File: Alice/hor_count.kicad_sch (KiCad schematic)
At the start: 267 parts, among them Q1 PASS, Q159 NOT_OC, Q160 NOT_OC, Q161 NOT_OC, Q162 NOT_OC, Q163 NOT_OC, Q164 NOT_OC, Q165 NOT_OC, Q166 NOT_OC, Q167 NOT_OC, Q168 NOT_OC, Q169 NOT_OC, Q170 NOT_OC, Q171 NOT_OC, Q172 NOT_OC, Q173 NOT_OC, Q174 NOT_OC, Q175 NOT_OC, Q176 NOT_OC, Q177 NOT_OC, Q178 NOT_OC, Q179 NOT_OC, Q180 NOT_OC, Q181 NOT_OC, Q182 NOT_OC, Q183 NOT_OC, Q184 NOT_OC, Q185 NOT_OC, Q186 NOT_OC, Q187 NOT_OC, Q188 NOT_OC, Q189 NOT_OC, Q190 NOT_OC, Q191 NOT_OC, Q192 NOT_OC, Q193 NOT_OC, Q194 NOT_OC, Q195 NOT_OC, Q196 NOT_OC, Q197 NOT_OC, Q198 NOT_OC, Q199 NOT_OC, Q2 PASS, Q200 NOT_OC, Q201 NOT_OC, Q202 NOT_OC, Q203 NOT_OC, Q204 NOT_OC, Q205 NOT_OC, Q206 NOT_OC, Q207 NOT_OC, Q208 NOT_OC, Q209 NOT_OC, Q210 NOT_OC, Q211 NOT_OC, Q212 NOT_OC, Q213 NOT_OC, Q214 NOT_OC, Q215 NOT_OC, Q216 NOT_OC, Q217 NOT_OC, Q218 NOT_OC, Q219 NOT_OC, Q220 NOT_OC, Q221 NOT_OC, Q222 NOT_OC, Q223 NOT_OC, Q224 NOT_OC, Q225 NOT_OC, Q226 NOT_OC, Q227 NOT_OC, Q228 NOT_OC, Q229 NOT_OC, Q230 NOT_OC, Q231 NOT_OC, Q232 NOT_OC, Q233 NOT_OC, Q234 NOT_OC, Q235 NOT_OC, Q236 NOT_OC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

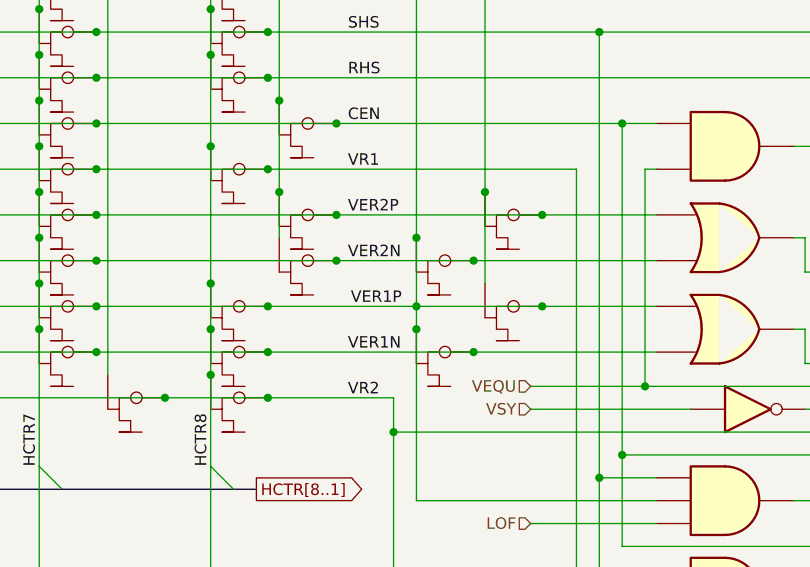
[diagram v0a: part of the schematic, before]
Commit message: Fixed a comb. loop in Alice schematics
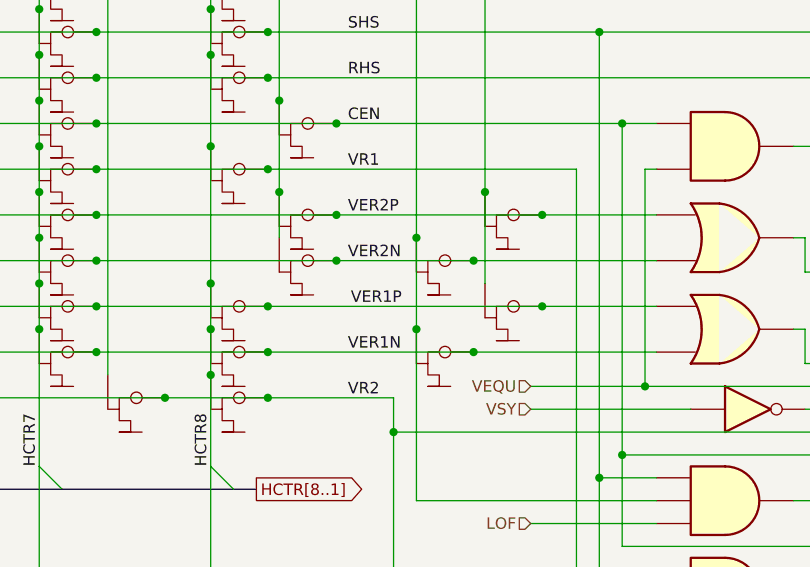
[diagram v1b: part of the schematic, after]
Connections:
- net PAL: no longer OR_2.2, Q164.1, Q182.1, Q192.1, Q208.1, Q220.1, Q233.1, Q247.1, Q257.1, Q269.1, R11.3 (D)
- new net VER1P: OR_2.2, Q164.1, Q182.1, Q192.1, Q208.1, Q220.1, Q233.1, Q247.1, Q257.1, Q269.1, R11.3 (D)
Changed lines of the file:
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@@
   (junction (at 88.9 238.76) (diameter 0) (color 0 0 0 0)
   )
-  (junction (at 207.01 137.16) (diameter 0) (color 0 0 0 0)
-  )
   (junction (at 57.15 127) (diameter 0) (color 0 0 0 0)
   )
@@
     (stroke (width 0) (type default) (color 0 0 0 0))
   )
-  (wire (pts (xy 190.5 137.16) (xy 207.01 137.16))
+  (wire (pts (xy 190.5 137.16) (xy 220.98 137.16))
     (stroke (width 0) (type default) (color 0 0 0 0))
   )
@@
     (stroke (width 0) (type default) (color 0 0 0 0))
   )
-  (wire (pts (xy 207.01 137.16) (xy 220.98 137.16))
-    (stroke (width 0) (type default) (color 0 0 0 0))
-  )
   (wire (pts (xy 289.56 241.3) (xy 293.37 241.3))
     (stroke (width 0) (type default) (color 0 0 0 0))
@@
     (stroke (width 0) (type default) (color 0 0 0 0))
   )
-  (wire (pts (xy 207.01 129.54) (xy 207.01 137.16))
+  (wire (pts (xy 207.01 129.54) (xy 207.01 139.7))
     (stroke (width 0) (type default) (color 0 0 0 0))
   )
@@
     (stroke (width 0) (type default) (color 0 0 0 0))
   )
-  (wire (pts (xy 207.01 137.16) (xy 207.01 139.7))
-    (stroke (width 0) (type default) (color 0 0 0 0))
-  )

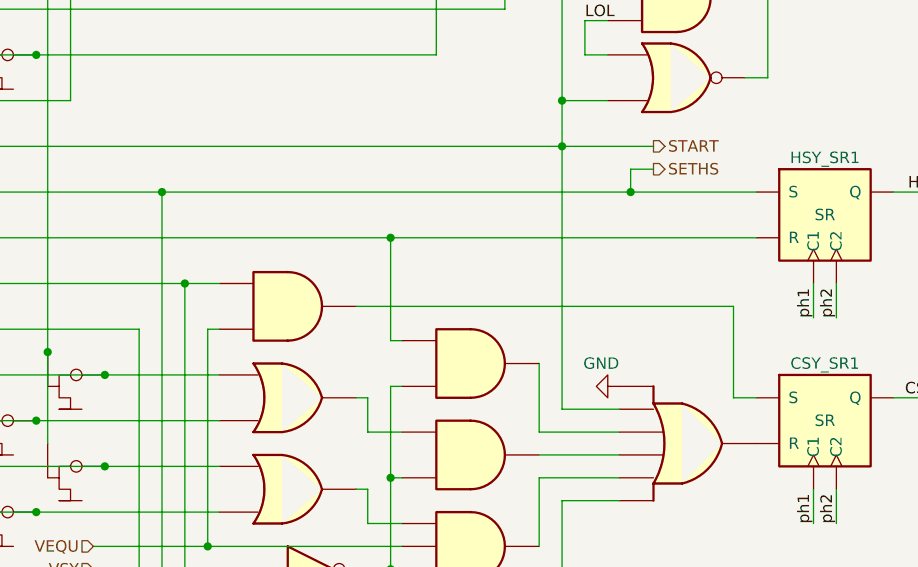
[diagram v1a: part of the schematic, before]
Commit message: Fixed synchros generation
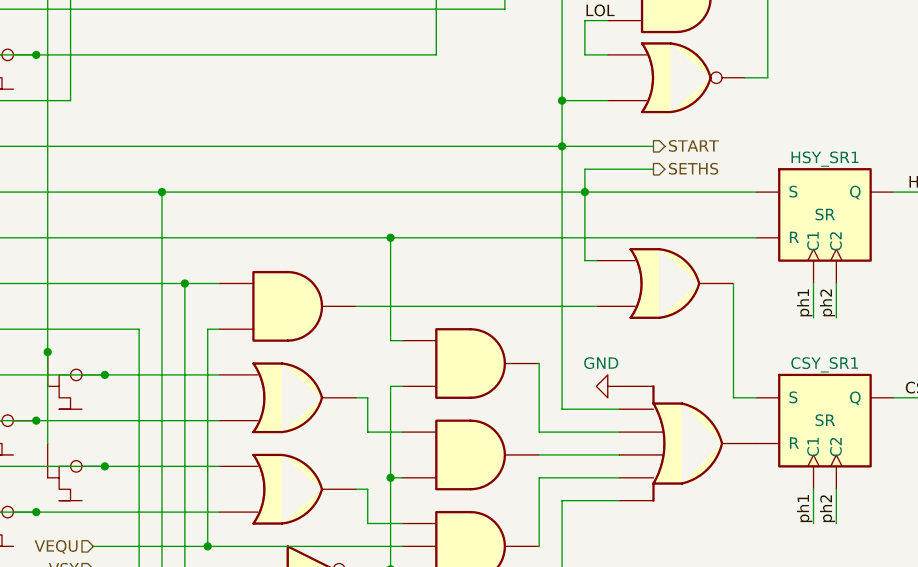
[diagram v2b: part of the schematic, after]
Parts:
- added OR_21: OR2, symbol NMOS:OR2
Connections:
- net SETHS: now also OR_21.2
- net at AND_4.1: now also OR_21.3; no longer CSY_SR1.7 (S)
- new net: CSY_SR1.7 (S), OR_21.1
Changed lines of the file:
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@@
   (junction (at 62.23 238.76) (diameter 0) (color 0 0 0 0)
   )
+  (junction (at 274.32 106.68) (diameter 0) (color 0 0 0 0)
+  )
   (junction (at 57.15 265.43) (diameter 0) (color 0 0 0 0)
   )
@@
   (junction (at 157.48 203.2) (diameter 0) (color 0 0 0 0)
   )
-  (junction (at 279.4 106.68) (diameter 0) (color 0 0 0 0)
-  )
   (junction (at 88.9 139.7) (diameter 0) (color 0 0 0 0)
   )
@@
     (stroke (width 0) (type default) (color 0 0 0 0))
   )
-  (wire (pts (xy 248.92 119.38) (xy 290.83 119.38))
+  (wire (pts (xy 248.92 119.38) (xy 275.59 119.38))
     (stroke (width 0) (type default) (color 0 0 0 0))
   )
@@
     (stroke (width 0) (type default) (color 0 0 0 0))
   )
-  (wire (pts (xy 290.83 129.54) (xy 290.83 119.38))
+  (wire (pts (xy 290.83 116.84) (xy 290.83 129.54))
     (stroke (width 0) (type default) (color 0 0 0 0))
   )
@@
     (stroke (width 0) (type default) (color 0 0 0 0))
   )
-  (wire (pts (xy 279.4 106.68) (xy 293.37 106.68))
-    (stroke (width 0) (type default) (color 0 0 0 0))
-  )
   (wire (pts (xy 189.23 250.19) (xy 198.12 250.19))
     (stroke (width 0) (type default) (color 0 0 0 0))
@@
     (stroke (width 0) (type default) (color 0 0 0 0))
   )
-  (wire (pts (xy 281.94 104.14) (xy 279.4 104.14))
+  (wire (pts (xy 281.94 104.14) (xy 274.32 104.14))
     (stroke (width 0) (type default) (color 0 0 0 0))
   )
@@
     (stroke (width 0) (type default) (color 0 0 0 0))
   )
+  (wire (pts (xy 274.32 106.68) (xy 274.32 114.3))
+    (stroke (width 0) (type default) (color 0 0 0 0))
+  )
   (wire (pts (xy 292.1 76.2) (xy 294.64 76.2))
     (stroke (width 0) (type default) (color 0 0 0 0))
@@
     (stroke (width 0) (type default) (color 0 0 0 0))
   )
-  (wire (pts (xy 279.4 104.14) (xy 279.4 106.68))
+  (wire (pts (xy 274.32 104.14) (xy 274.32 106.68))
     (stroke (width 0) (type default) (color 0 0 0 0))
   )
@@
     (stroke (width 0) (type default) (color 0 0 0 0))
   )
+  (wire (pts (xy 274.32 106.68) (xy 293.37 106.68))
+    (stroke (width 0) (type default) (color 0 0 0 0))
+  )
   (wire (pts (xy 45.72 147.32) (xy 64.77 147.32))
     (stroke (width 0) (type default) (color 0 0 0 0))
@@
     (stroke (width 0) (type default) (color 0 0 0 0))
   )
+  (wire (pts (xy 275.59 114.3) (xy 274.32 114.3))
+    (stroke (width 0) (type default) (color 0 0 0 0))
+  )
   (wire (pts (xy 213.36 132.08) (xy 233.68 132.08))
     (stroke (width 0) (type default) (color 0 0 0 0))
@@
     (stroke (width 0) (type default) (color 0 0 0 0))
   )
-  (wire (pts (xy 227.33 106.68) (xy 279.4 106.68))
+  (wire (pts (xy 227.33 106.68) (xy 274.32 106.68))
     (stroke (width 0) (type default) (color 0 0 0 0))
   )
@@
     (pin "6")
   )
+  (symbol (lib_id "NMOS:OR2") (at 283.21 116.84 0) (unit 1)
+    (in_bom yes) (on_board yes) (fields_autoplaced)
+    (property "Reference" "OR_21" (id 0) (at 283.21 116.84 0)
+      (effects (font (size 1.27 1.27)) hide)
+    )
+    (property "Value" "OR2" (id 1) (at 283.21 121.92 0)
+      (effects (font (size 1.27 1.27)) hide)
+    )
+    (property "Footprint" "" (id 2) (at 283.21 116.84 0)
+      (effects (font (size 1.27 1.27)) hide)
+    )
+    (property "Datasheet" "" (id 3) (at 283.21 116.84 0)
+      (effects (font (size 1.27 1.27)) hide)
+    )
+    (pin "1")
+    (pin "2")
+    (pin "3")
+  )
   (symbol (lib_id "NMOS:NOT_OC") (at 184.15 143.51 0) (unit 1)

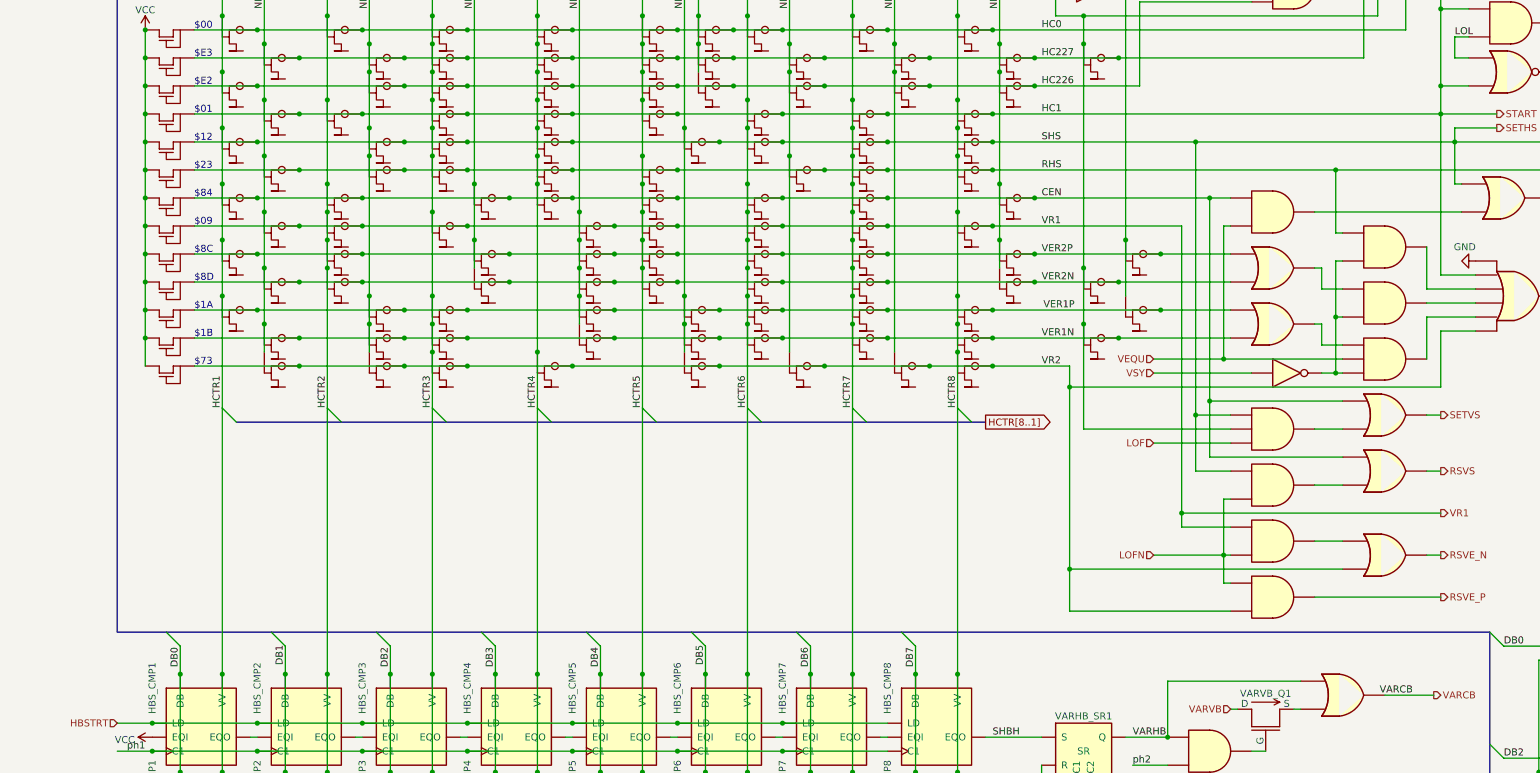
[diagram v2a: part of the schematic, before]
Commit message: Fixed DMA sheet added (partial)
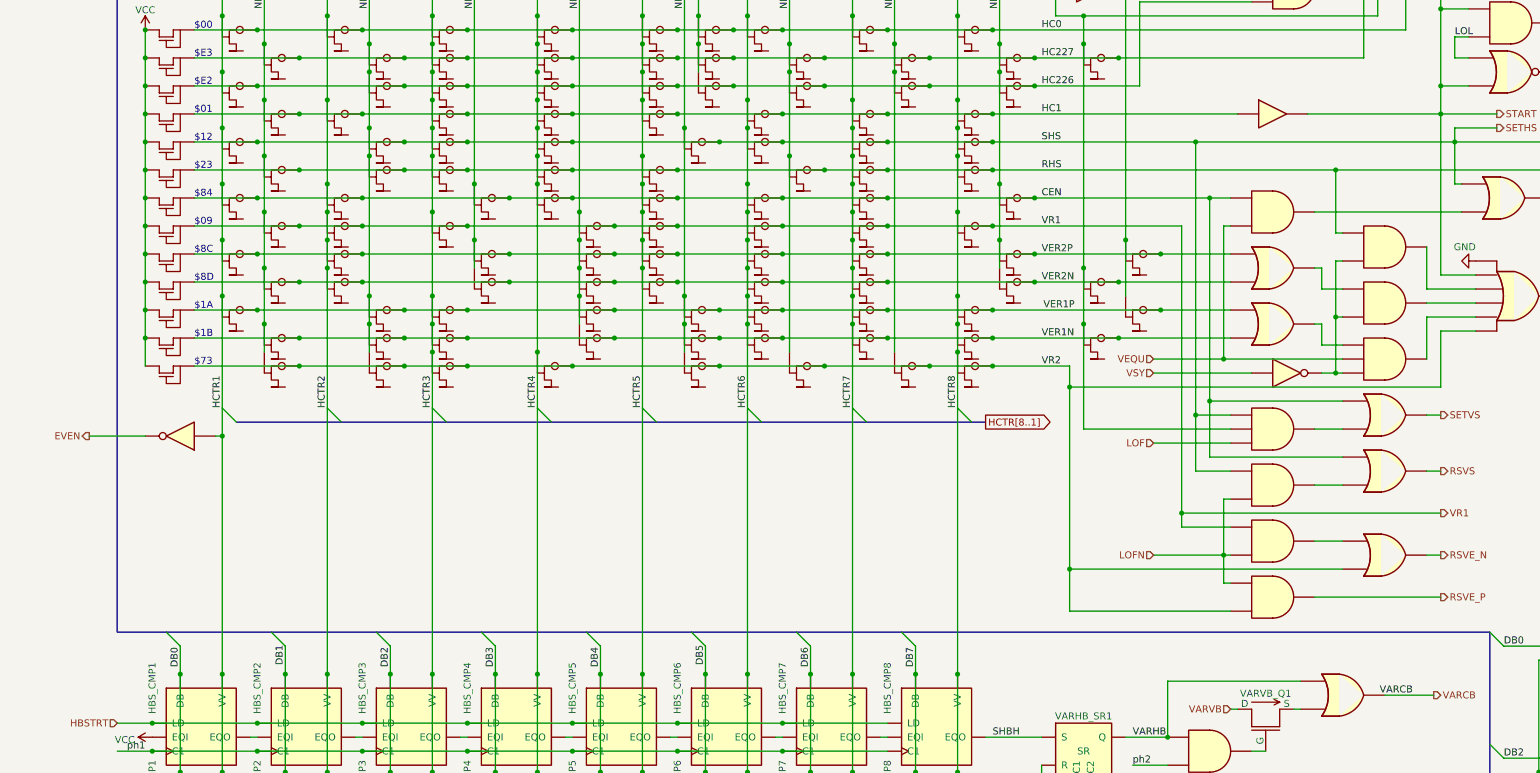
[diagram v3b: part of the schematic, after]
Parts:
- added BUF_1: BUF, symbol NMOS:BUF
- added NOT_10: NOT, symbol NMOS:NOT
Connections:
- net HCTR1: now also NOT_10.2
- net START: now also BUF_1.1; no longer Q166.1, Q173.1, Q188.1, Q201.1, Q213.1, Q227.1, Q240.1, Q253.1, R4.3 (D)
- new net EVEN: NOT_10.1
- new net HC1: BUF_1.2, Q166.1, Q173.1, Q188.1, Q201.1, Q213.1, Q227.1, Q240.1, Q253.1, R4.3 (D)
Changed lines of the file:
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@@
   (junction (at 36.83 116.84) (diameter 0) (color 0 0 0 0)
   )
+  (junction (at 50.8 160.02) (diameter 0) (color 0 0 0 0)
+  )
   (junction (at 88.9 83.82) (diameter 0) (color 0 0 0 0)
   )
@@
     (stroke (width 0) (type default) (color 0 0 0 0))
   )
+  (wire (pts (xy 49.53 160.02) (xy 50.8 160.02))
+    (stroke (width 0) (type default) (color 0 0 0 0))
+  )
   (wire (pts (xy 45.72 68.58) (xy 64.77 68.58))
     (stroke (width 0) (type default) (color 0 0 0 0))
@@
     (stroke (width 0) (type default) (color 0 0 0 0))
   )
-  (wire (pts (xy 50.8 154.94) (xy 50.8 203.2))
+  (wire (pts (xy 50.8 154.94) (xy 50.8 160.02))
     (stroke (width 0) (type default) (color 0 0 0 0))
   )
@@
     (stroke (width 0) (type default) (color 0 0 0 0))
   )
+  (wire (pts (xy 26.67 160.02) (xy 36.83 160.02))
+    (stroke (width 0) (type default) (color 0 0 0 0))
+  )
   (bus (pts (xy 129.54 157.48) (xy 148.59 157.48))
     (stroke (width 0) (type default) (color 0 0 0 0))
@@
     (stroke (width 0) (type default) (color 0 0 0 0))
   )
+  (wire (pts (xy 247.65 101.6) (xy 271.78 101.6))
+    (stroke (width 0) (type default) (color 0 0 0 0))
+  )
   (wire (pts (xy 204.47 151.13) (xy 271.78 151.13))
     (stroke (width 0) (type default) (color 0 0 0 0))
@@
     (stroke (width 0) (type default) (color 0 0 0 0))
   )
-  (wire (pts (xy 190.5 101.6) (xy 271.78 101.6))
+  (wire (pts (xy 190.5 101.6) (xy 234.95 101.6))
     (stroke (width 0) (type default) (color 0 0 0 0))
   )
@@
     (stroke (width 0) (type default) (color 0 0 0 0))
   )
+  (wire (pts (xy 50.8 160.02) (xy 50.8 203.2))
+    (stroke (width 0) (type default) (color 0 0 0 0))
+  )
   (wire (pts (xy 215.9 219.71) (xy 222.25 219.71))
     (stroke (width 0) (type default) (color 0 0 0 0))
@@
     (effects (font (size 1.27 1.27)) (justify right))
   )
+  (hierarchical_label "EVEN" (shape output) (at 26.67 160.02 180)
+    (effects (font (size 1.27 1.27)) (justify right))
+  )
   (hierarchical_label "LP_HVL" (shape input) (at 26.67 25.4 180)
     (effects (font (size 1.27 1.27)) (justify right))
@@
     (pin "3")
   )
+  (symbol (lib_id "NMOS:NOT") (at 43.18 160.02 180) (unit 1)
+    (in_bom yes) (on_board yes) (fields_autoplaced)
+    (property "Reference" "NOT_10" (id 0) (at 43.18 163.83 0)
+      (effects (font (size 1.27 1.27)) hide)
+    )
+    (property "Value" "NOT" (id 1) (at 43.18 154.94 0)
+      (effects (font (size 1.27 1.27)) hide)
+    )
+    (property "Footprint" "" (id 2) (at 43.18 160.02 0)
+      (effects (font (size 1.27 1.27)) hide)
+    )
+    (property "Datasheet" "" (id 3) (at 43.18 160.02 0)
+      (effects (font (size 1.27 1.27)) hide)
+    )
+    (pin "1")
+    (pin "2")
+  )
   (symbol (lib_id "NMOS:MUX") (at 392.43 231.14 0) (unit 1)
     (in_bom yes) (on_board yes) (fields_autoplaced)
@@
     (pin "3")
   )
+  (symbol (lib_id "NMOS:BUF") (at 241.3 101.6 0) (unit 1)
+    (in_bom yes) (on_board yes) (fields_autoplaced)
+    (property "Reference" "BUF_1" (id 0) (at 241.3 97.79 0)
+      (effects (font (size 1.27 1.27)) hide)
+    )
+    (property "Value" "BUF" (id 1) (at 241.3 106.68 0)
+      (effects (font (size 1.27 1.27)) hide)
+    )
+    (property "Footprint" "" (id 2) (at 241.3 101.6 0)
+      (effects (font (size 1.27 1.27)) hide)
+    )
+    (property "Datasheet" "" (id 3) (at 241.3 101.6 0)
+      (effects (font (size 1.27 1.27)) hide)
+    )
+    (pin "1")
+    (pin "2")
+  )
   (symbol (lib_id "NMOS:NOT_OC") (at 165.1 118.11 0) (unit 1)

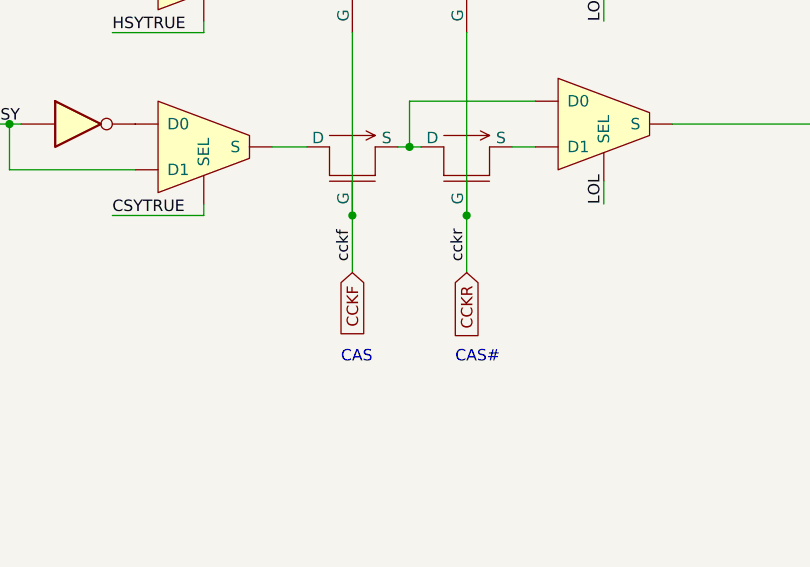
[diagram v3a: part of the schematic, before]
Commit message: Fixed CAS clock polarity, added DMA priority logic
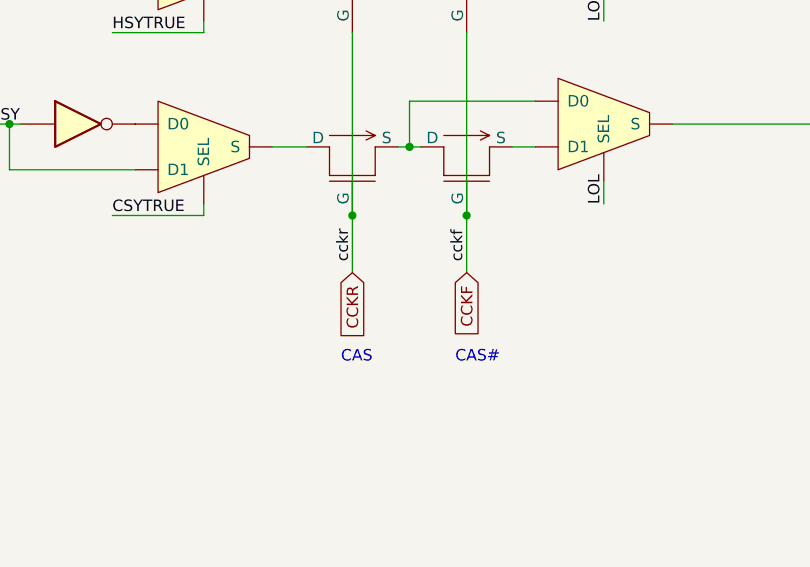
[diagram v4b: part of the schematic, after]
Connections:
- net CCKF: now also Q2.2 (G), Q4.2 (G); no longer Q1.2 (G), Q3.2 (G)
- net CCKR: now also Q1.2 (G), Q3.2 (G); no longer Q2.2 (G), Q4.2 (G)
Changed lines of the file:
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@@
-    (effects (font (size 1.27 1.27)) (justify left bottom))
-  )
-  (label "cckf" (at 408.94 264.16 90)
     (effects (font (size 1.27 1.27)) (justify left bottom))
   )
@@
     (effects (font (size 1.27 1.27)) (justify left bottom))
   )
+  (label "cckf" (at 421.64 264.16 90)
+    (effects (font (size 1.27 1.27)) (justify left bottom))
+  )
   (label "DHEND" (at 231.14 285.75 0)
     (effects (font (size 1.27 1.27)) (justify left bottom))
@@
     (effects (font (size 1.27 1.27)) (justify left bottom))
   )
+  (label "cckr" (at 408.94 264.16 90)
+    (effects (font (size 1.27 1.27)) (justify left bottom))
+  )
   (label "ph1" (at 36.83 270.51 180)
     (effects (font (size 1.27 1.27)) (justify right bottom))
@@
   )
   (label "HCTR2" (at 69.85 154.94 90)
-    (effects (font (size 1.27 1.27)) (justify left bottom))
-  )
-  (label "cckr" (at 421.64 264.16 90)
     (effects (font (size 1.27 1.27)) (justify left bottom))
   )
@@
     )
   )
-  (global_label "CCKF" (shape input) (at 408.94 265.43 270) (fields_autoplaced)
-    (effects (font (size 1.27 1.27)) (justify right))
-    (property "Intersheet References" "${INTERSHEET_REFS}" (id 0) (at 408.8606 272.7417 90)
-      (effects (font (size 1.27 1.27)) (justify right) hide)
-    )
-  )
   (global_label "PHI2" (shape input) (at 26.67 68.58 180) (fields_autoplaced)
     (effects (font (size 1.27 1.27)) (justify right))
     (property "Intersheet References" "${INTERSHEET_REFS}" (id 0) (at 19.8421 68.5006 0)
+      (effects (font (size 1.27 1.27)) (justify right) hide)
+    )
+  )
+  (global_label "CCKR" (shape input) (at 408.94 265.43 270) (fields_autoplaced)
+    (effects (font (size 1.27 1.27)) (justify right))
+    (property "Intersheet References" "${INTERSHEET_REFS}" (id 0) (at 408.8606 272.9231 90)
       (effects (font (size 1.27 1.27)) (justify right) hide)
     )
@@
     )
   )
-  (global_label "CCKR" (shape input) (at 421.64 265.43 270) (fields_autoplaced)
-    (effects (font (size 1.27 1.27)) (justify right))
-    (property "Intersheet References" "${INTERSHEET_REFS}" (id 0) (at 421.5606 272.9231 90)
-      (effects (font (size 1.27 1.27)) (justify right) hide)
-    )
-  )
   (global_label "CSYNC" (shape output) (at 464.82 248.92 0) (fields_autoplaced)
     (effects (font (size 1.27 1.27)) (justify left))
@@
       (effects (font (size 1.27 1.27)) (justify right) hide)
     )
+  )
+  (global_label "CCKF" (shape input) (at 421.64 265.43 270) (fields_autoplaced)
+    (effects (font (size 1.27 1.27)) (justify right))
+    (property "Intersheet References" "${INTERSHEET_REFS}" (id 0) (at 421.5606 272.7417 90)
+      (effects (font (size 1.27 1.27)) (justify right) hide)
+    )
